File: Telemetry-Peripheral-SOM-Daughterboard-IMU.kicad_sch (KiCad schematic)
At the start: 3 parts, among them J1 Conn_02x10_Odd_Even

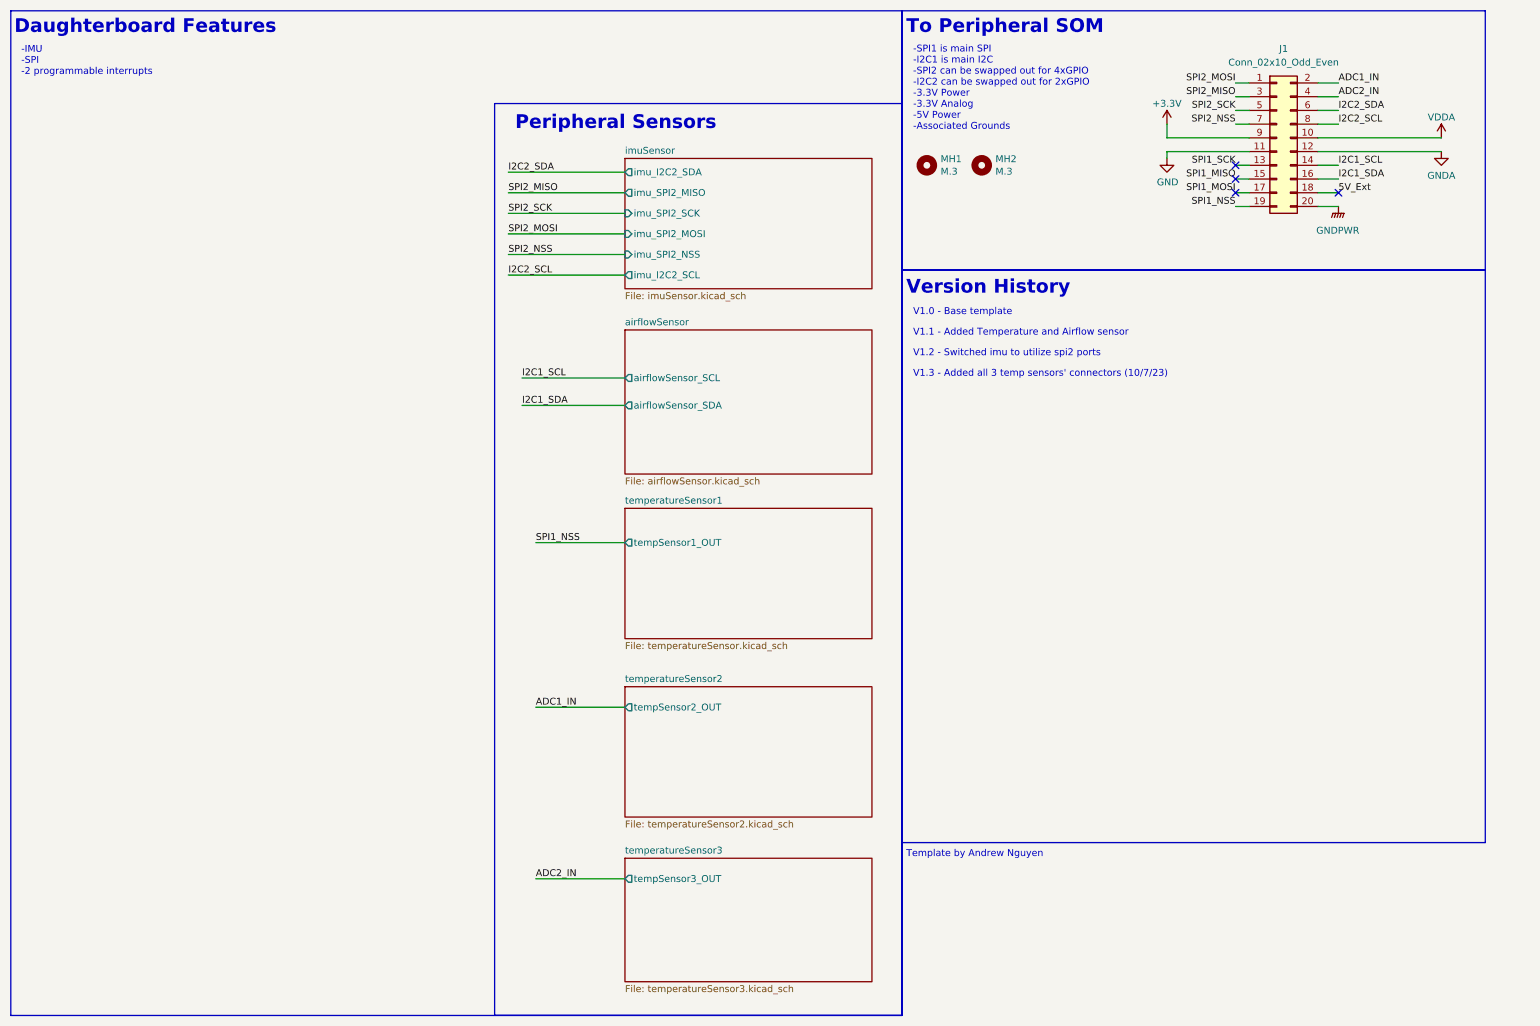
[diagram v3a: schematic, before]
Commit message: added test points in schematic
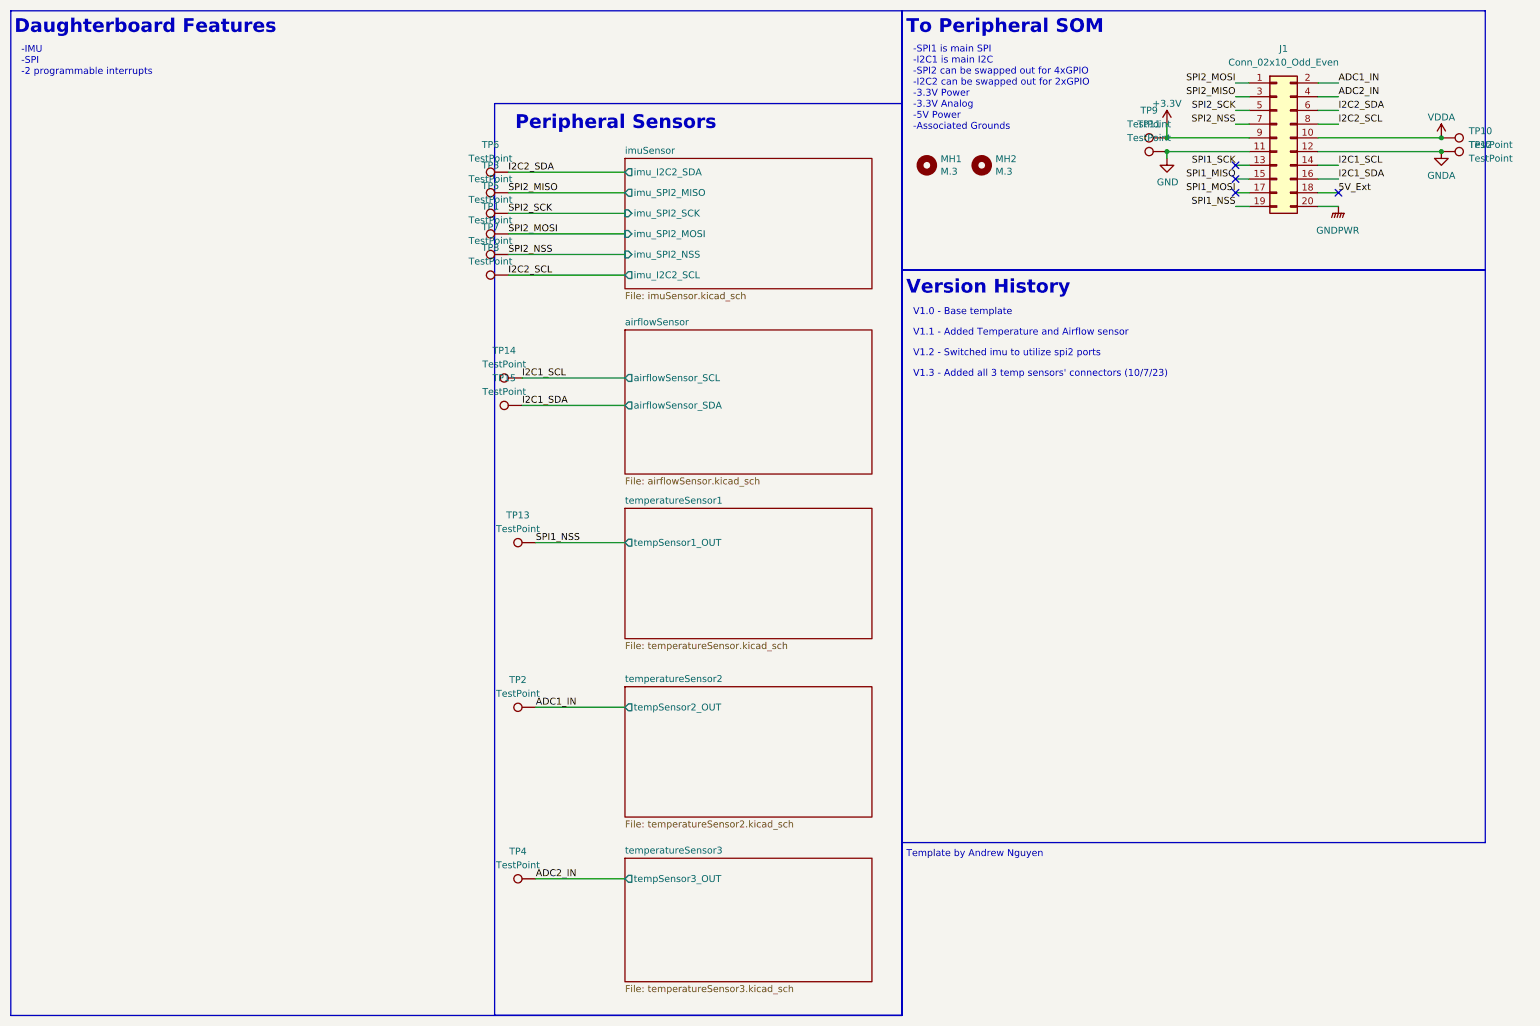
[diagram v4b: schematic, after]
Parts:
- added TP1, TP10, TP11, TP12, TP13, TP14, TP15, TP2, TP3, TP4, TP5, TP6, TP7, TP8, TP9: TestPoint, symbol Connector:TestPoint
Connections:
- net +3.3V: now also TP9.1
- net ADC1_IN: now also TP2.1
- net ADC2_IN: now also TP4.1
- net GND: now also TP11.1
- net GNDA: now also TP12.1
- net I2C1_SCL: now also TP14.1
- net I2C1_SDA: now also TP15.1
- net I2C2_SCL: now also TP8.1
- net I2C2_SDA: now also TP6.1
- net SPI1_NSS: now also TP13.1
- net SPI2_MISO: now also TP3.1
- net SPI2_MOSI: now also TP1.1
- net SPI2_NSS: now also TP7.1
- net SPI2_SCK: now also TP5.1
- net VDDA: now also TP10.1

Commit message: fixes
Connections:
- net ADC1_IN: no longer TP2.1
- net ADC2_IN: no longer TP4.1
- net I2C1_SCL: now also TP8.1; no longer TP14.1
- net I2C1_SDA: now also TP6.1; no longer TP15.1
- net I2C2_SCL: now also TP14.1; no longer TP8.1
- net I2C2_SDA: now also TP15.1; no longer TP6.1
- net SPI1_MISO: now also TP3.1
- net SPI1_MOSI: now also TP1.1
- net SPI1_NSS: now also TP7.1; no longer TP13.1
- net SPI1_SCK: now also TP5.1
- net SPI2_MISO: no longer TP3.1
- net SPI2_MOSI: no longer TP1.1
- net SPI2_NSS: no longer TP7.1
- net SPI2_SCK: no longer TP5.1
- new net temperatureSensor1/tempSensor1_OUT: TP13.1
- new net temperatureSensor2/tempSensor2_OUT: TP2.1
- new net temperatureSensor3/tempSensor3_OUT: TP4.1
- no-connect marks 4 -> 1
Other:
- sheet imuSensor ports: added CS, INT1, INT2, SCL, SDA, SDO/SA0; removed imu_I2C2_SCL, imu_I2C2_SDA, imu_SPI2_MISO, imu_SPI2_MOSI, imu_SPI2_NSS, imu_SPI2_SCK
- note added: "BPS opening up pins 18 and 20"
- note added: "Need to add pull up resistors for I2C2 (not on BPS board)"
- note added: "a third one is needed"
- moved on the sheet: TP10, TP11, TP12, TP13, TP14, TP15, TP2, TP4, TP9

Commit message: revision
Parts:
- removed TP1, TP10, TP11, TP12, TP13, TP14, TP15, TP2, TP3, TP4, TP5, TP6, TP7, TP8, TP9: TestPoint, symbol Connector:TestPoint
- added 3.3V_TP1, GND_TP1: TestPoint, TestPoint:TestPoint_Pad_2.0x2.0mm, symbol Connector:TestPoint
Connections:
- net ADC1_IN is gone; now on net +3.3V: J1.2 (Pin_2)
- net ADC2_IN is gone; now on net GND: J1.4 (Pin_4)
- net +3.3V: now also 3.3V_TP1.1
- net GND: now also GND_TP1.1
- net 5V_Ext renamed +5V
- no-connect marks 1 -> 3

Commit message: Integrated changes made by BPS
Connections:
- net +5V renamed PA2
- net GNDPWR renamed PA1
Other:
- note added: "PA1 and PA2 are ADC pins opened up by BPS"
- note added: "Pull out resistors are on BPS Leader SOM"
- note added: "SPI1_NSS has additional ADC functionality"
- note added: "V1.4 -"
- note removed: "BPS opening up pins 18 and 20"
- note removed: "Need to add pull up resistors for I2C2 (not on BPS board)"
- note removed: "a third one is needed"
- moved on the sheet: 3.3V_TP1, GND_TP1

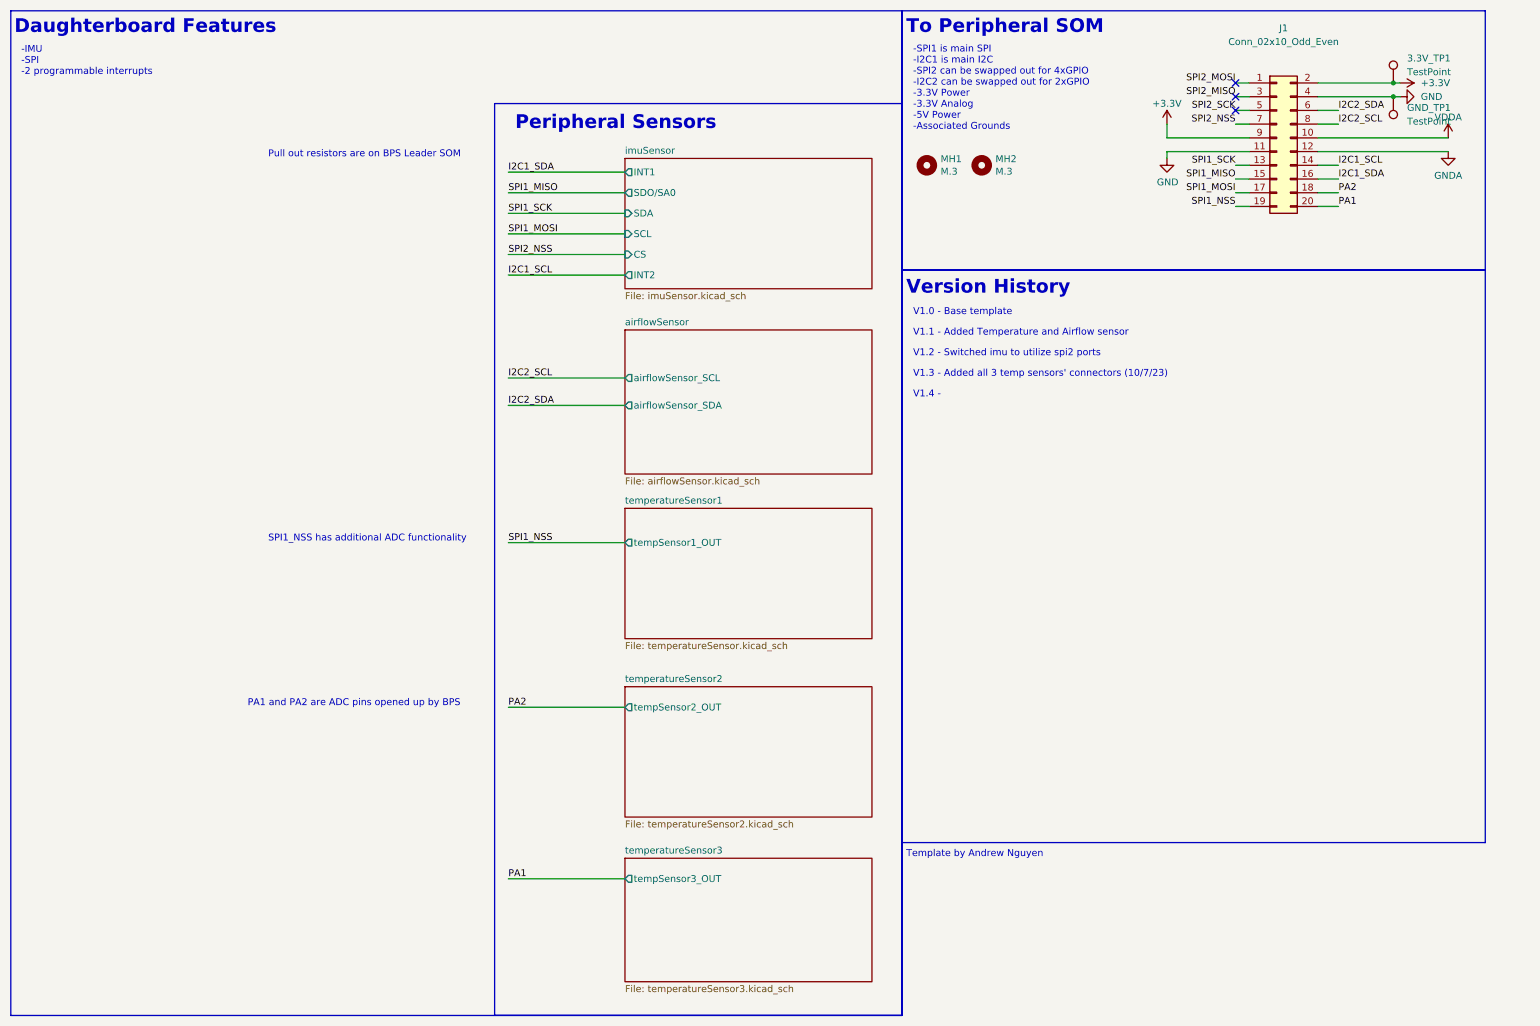
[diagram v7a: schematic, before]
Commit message: added protective circuitry for temp sensors, made name changes for IMU
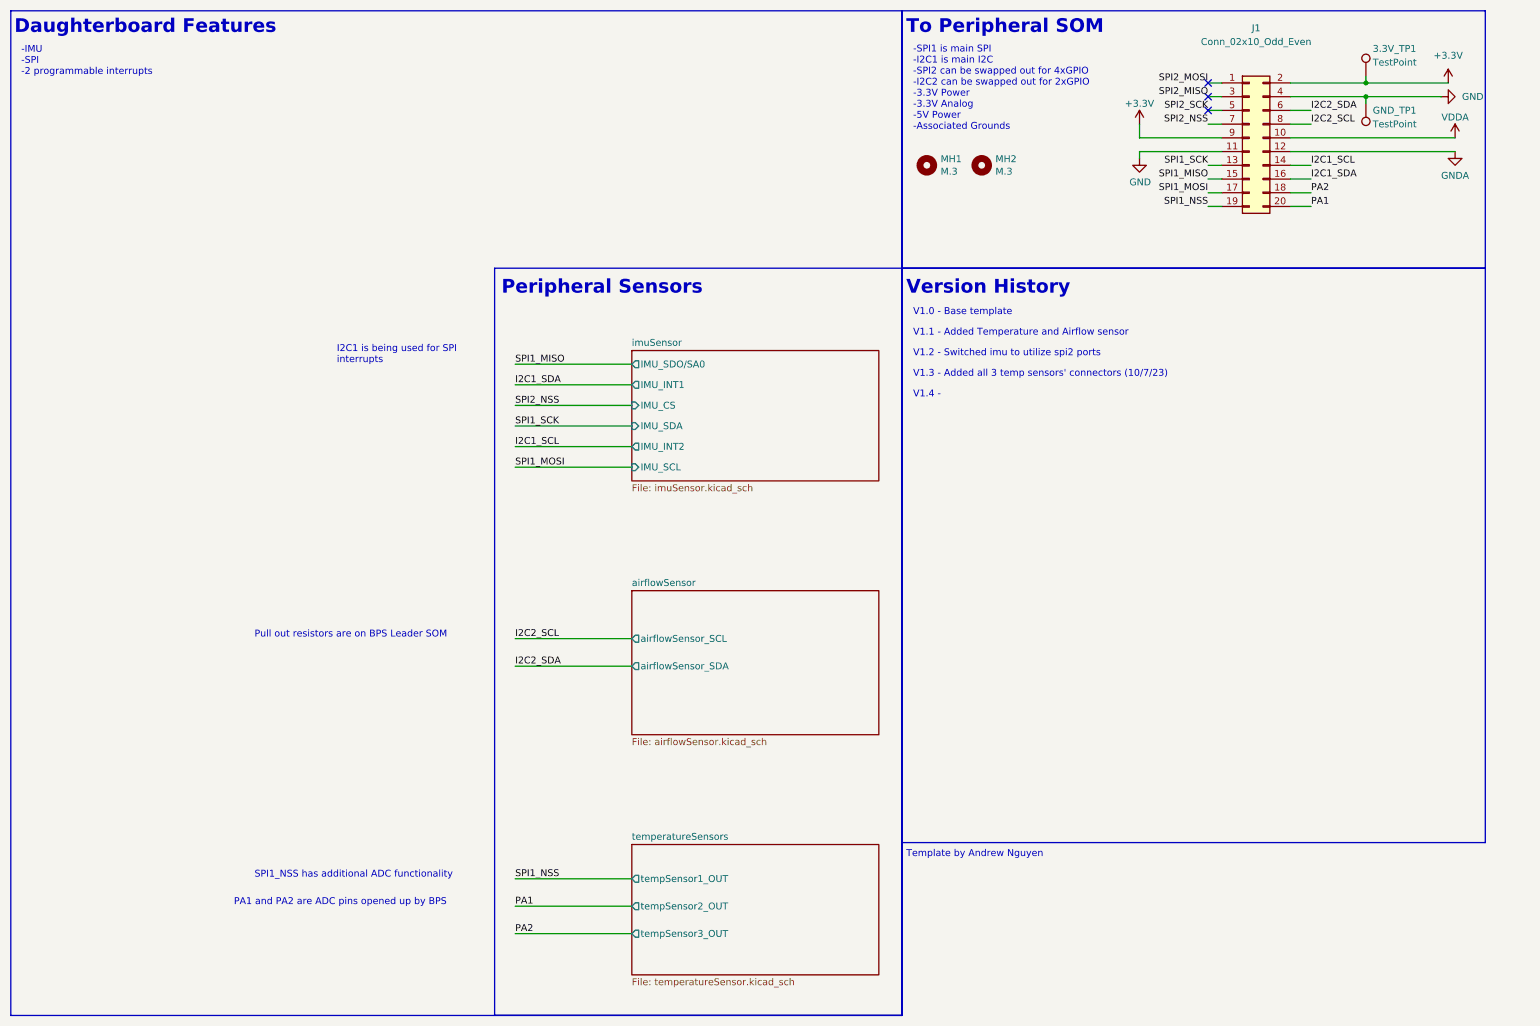
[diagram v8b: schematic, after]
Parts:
- J1: Manufacturer_Name (none) -> Molex; Mouser Part Number (none) -> 538-53307-2071
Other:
- sheet temperatureSensor1 renamed temperatureSensors
- removed sheet temperatureSensor2
- removed sheet temperatureSensor3
- sheet imuSensor ports: added IMU_CS, IMU_INT1, IMU_INT2, IMU_SCL, IMU_SDA, IMU_SDO/SA0; removed CS, INT1, INT2, SCL, SDA, SDO/SA0
- sheet temperatureSensors ports: added tempSensor2_OUT, tempSensor3_OUT; removed none
- note added: "I2C1 is being used for SPI interrupts"
- moved on the sheet: 3.3V_TP1, GND_TP1, J1
